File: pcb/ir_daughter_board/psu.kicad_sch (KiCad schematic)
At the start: 12 parts, among them IC1 TS2596SCS

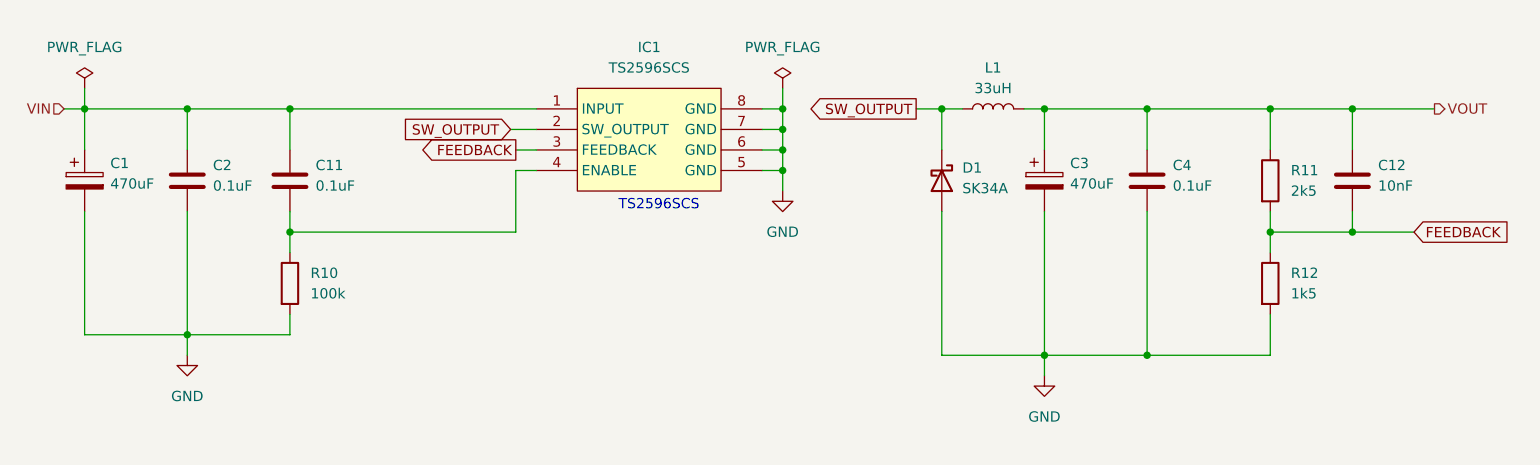
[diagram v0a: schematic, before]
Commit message: refined circuit with reddit comments
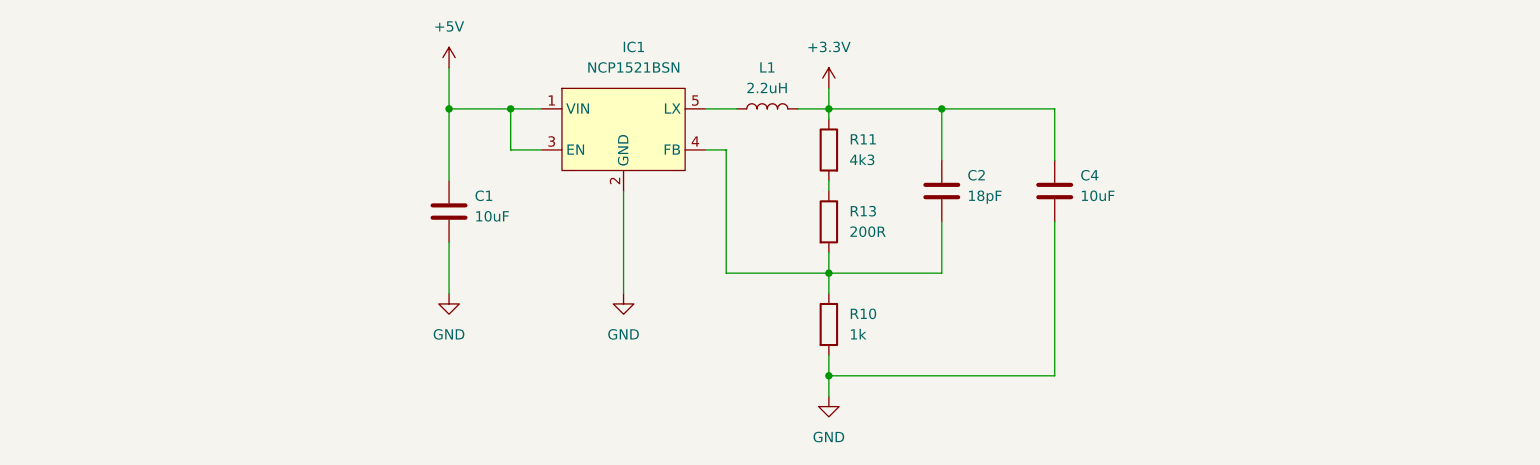
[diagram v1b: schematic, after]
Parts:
- removed C1, C3: 470uF, Capacitor_SMD:C_0603_1608Metric, symbol Device:C_Polarized
- removed C11: 0.1uF, Capacitor_SMD:C_0603_1608Metric, symbol Device:C
- removed C12: 10nF, Capacitor_SMD:C_0603_1608Metric, symbol Device:C
- removed D1: SK34A, Diode_SMD:D_SMA, symbol Device:D_Schottky
- removed IC1: TS2596SCS, Package_SO:SO-8_3.9x4.9mm_P1.27mm, symbol TS2596CM533_RNG:TS2596SCS
- removed R12: 1k5, Resistor_SMD:R_0603_1608Metric, symbol Device:R
- added C1: 10uF, Capacitor_SMD:C_0603_1608Metric, symbol Device:C
- added IC1: NCP1521BSN, Package_SO:TSOP-5_1.65x3.05mm_P0.95mm, symbol NCP1521BSN:NCP1521BSN
- added R13: 200R, Resistor_SMD:R_0603_1608Metric, symbol Device:R
- C2: value 0.1uF -> 18pF
- C4: value 0.1uF -> 10uF
- L1: value 33uH -> 2.2uH
- R10: value 100k -> 1k
- R11: value 2k5 -> 4k3
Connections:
- net VOUT is gone; now on net +3V3: C4.1, L1.2, R11.1
- net GND: now also C1.2, IC1.2 (GND); no longer C2.2
- net at R10.1: now also C2.2, IC1.4 (FB), R13.2
- net FEEDBACK: no longer names the net of R11.2
- net FEEDBACK: now also R13.1
- net SW_OUTPUT: no longer names the net of L1.1
- net SW_OUTPUT: now also IC1.5 (LX)
- net VIN renamed +3V3
- new net +5V: C1.1, IC1.1 (VIN), IC1.3 (EN)
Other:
- note removed: "TS2596SCS"
- moved on the sheet: C4, L1, R11

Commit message: adapted pcb due to parts availability
Signed-off-by: LehrChristoph <christoph.lehr@gmx.at>
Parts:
- C1: value 10uF -> 4.7uF; footprint Capacitor_SMD:C_0603_1608Metric -> Capacitor_SMD:C_1210_3225Metric
- L1: footprint Inductor_SMD:L_1206_3216Metric -> Inductor_SMD:L_1210_3225Metric
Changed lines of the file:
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@@
       (effects (font (size 1.27 1.27)) (justify left))
     )
-    (property "Value" "10uF" (id 1) (at 94.615 64.135 0)
+    (property "Value" "4.7uF" (id 1) (at 94.615 64.135 0)
       (effects (font (size 1.27 1.27)) (justify left))
     )
-    (property "Footprint" "Capacitor_SMD:C_0603_1608Metric" (id 2) (at 92.4052 67.31 0)
+    (property "Footprint" "Capacitor_SMD:C_1210_3225Metric" (id 2) (at 92.4052 67.31 0)
       (effects (font (size 1.27 1.27)) hide)
     )
@@
     (property "Reference" "L1" (id 0) (at 130.81 45.72 90))
     (property "Value" "2.2uH" (id 1) (at 130.81 48.26 90))
-    (property "Footprint" "Inductor_SMD:L_1206_3216Metric" (id 2) (at 130.81 50.8 0)
+    (property "Footprint" "Inductor_SMD:L_1210_3225Metric" (id 2) (at 130.81 50.8 0)
       (effects (font (size 1.27 1.27)) hide)
     )

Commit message: minor updateds in references and values
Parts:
- renumbered C4 to C3, R11 to R1, R13 to R2, R10 to R3
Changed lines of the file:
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@@
   (symbol (lib_id "power:GND") (at 91.44 73.66 0) (unit 1)
     (in_bom yes) (on_board yes) (fields_autoplaced)
-    (property "Reference" "#PWR03" (id 0) (at 91.44 80.01 0)
+    (property "Reference" "#PWR07" (id 0) (at 91.44 80.01 0)
       (effects (font (size 1.27 1.27)) hide)
     )
@@
   (symbol (lib_id "Device:C") (at 166.37 60.96 0) (unit 1)
     (in_bom yes) (on_board yes)
-    (property "Reference" "C4" (id 0) (at 169.545 59.055 0)
+    (property "Reference" "C3" (id 0) (at 169.545 59.055 0)
       (effects (font (size 1.27 1.27)) (justify left))
     )
@@
   (symbol (lib_id "power:+3.3V") (at 138.43 48.26 0) (unit 1)
     (in_bom yes) (on_board yes) (fields_autoplaced)
-    (property "Reference" "#PWR014" (id 0) (at 138.43 52.07 0)
+    (property "Reference" "#PWR09" (id 0) (at 138.43 52.07 0)
       (effects (font (size 1.27 1.27)) hide)
     )
@@
   (symbol (lib_id "power:+5V") (at 91.44 45.72 0) (unit 1)
     (in_bom yes) (on_board yes) (fields_autoplaced)
-    (property "Reference" "#PWR09" (id 0) (at 91.44 49.53 0)
+    (property "Reference" "#PWR06" (id 0) (at 91.44 49.53 0)
       (effects (font (size 1.27 1.27)) hide)
     )
@@
   (symbol (lib_id "Device:R") (at 138.43 77.47 0) (unit 1)
     (in_bom yes) (on_board yes) (fields_autoplaced)
-    (property "Reference" "R10" (id 0) (at 140.97 76.1999 0)
+    (property "Reference" "R3" (id 0) (at 140.97 76.1999 0)
       (effects (font (size 1.27 1.27)) (justify left))
     )
@@
   (symbol (lib_id "Device:R") (at 138.43 64.77 0) (unit 1)
     (in_bom yes) (on_board yes) (fields_autoplaced)
-    (property "Reference" "R13" (id 0) (at 140.97 63.4999 0)
+    (property "Reference" "R2" (id 0) (at 140.97 63.4999 0)
       (effects (font (size 1.27 1.27)) (justify left))
     )
@@
   (symbol (lib_id "power:GND") (at 138.43 86.36 0) (unit 1)
     (in_bom yes) (on_board yes) (fields_autoplaced)
-    (property "Reference" "#PWR05" (id 0) (at 138.43 92.71 0)
+    (property "Reference" "#PWR010" (id 0) (at 138.43 92.71 0)
       (effects (font (size 1.27 1.27)) hide)
     )
@@
   (symbol (lib_id "Device:R") (at 138.43 55.88 0) (mirror y) (unit 1)
     (in_bom yes) (on_board yes) (fields_autoplaced)
-    (property "Reference" "R11" (id 0) (at 140.97 54.6099 0)
+    (property "Reference" "R1" (id 0) (at 140.97 54.6099 0)
       (effects (font (size 1.27 1.27)) (justify right))
     )
@@
   (symbol (lib_id "power:GND") (at 113.03 73.66 0) (unit 1)
     (in_bom yes) (on_board yes) (fields_autoplaced)
-    (property "Reference" "#PWR04" (id 0) (at 113.03 80.01 0)
+    (property "Reference" "#PWR08" (id 0) (at 113.03 80.01 0)
       (effects (font (size 1.27 1.27)) hide)
     )
